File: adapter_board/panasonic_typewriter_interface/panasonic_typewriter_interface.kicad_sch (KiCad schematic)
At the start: 21 parts, among them J1 KMDGX-8S-AS, J2 Conn_02x03_Odd_Even, J3 Connector:Conn_01x05_Male, J4 Connector:Conn_01x04_Male, J5 Connector:Conn_01x04_Male, SW1 SW_SPDT

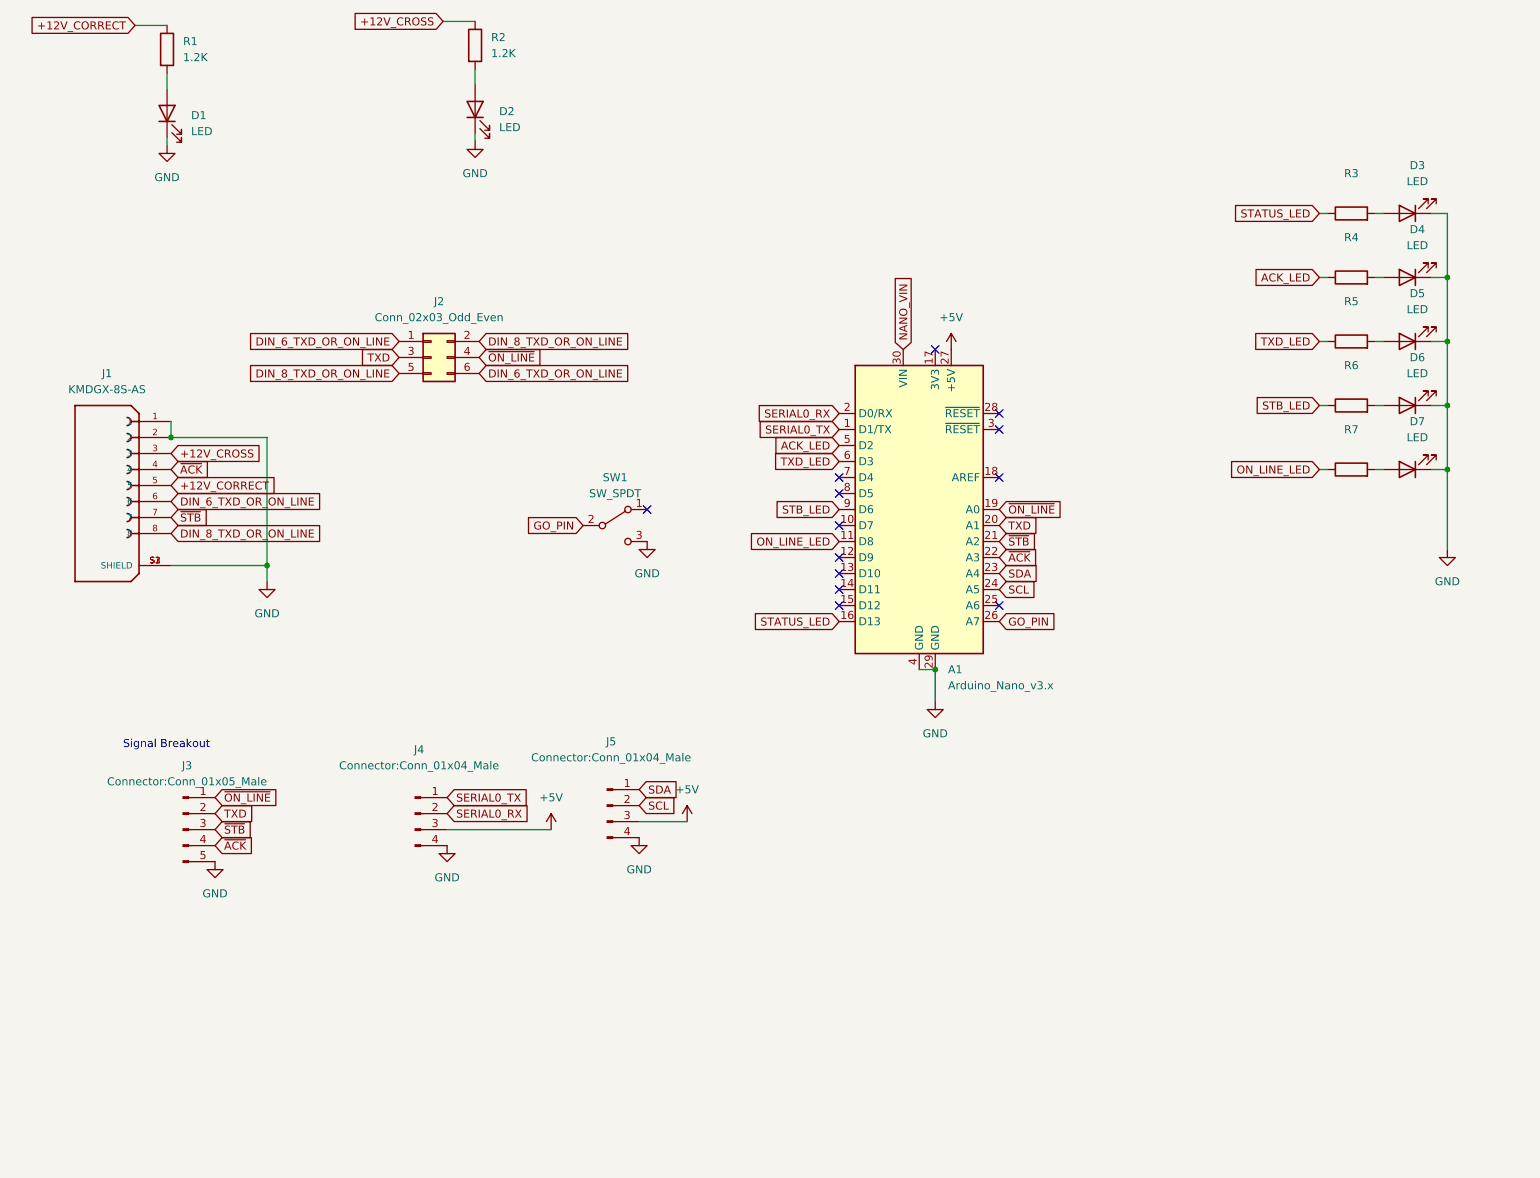
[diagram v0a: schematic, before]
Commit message: slightly larger board with mounting holes and an extra button
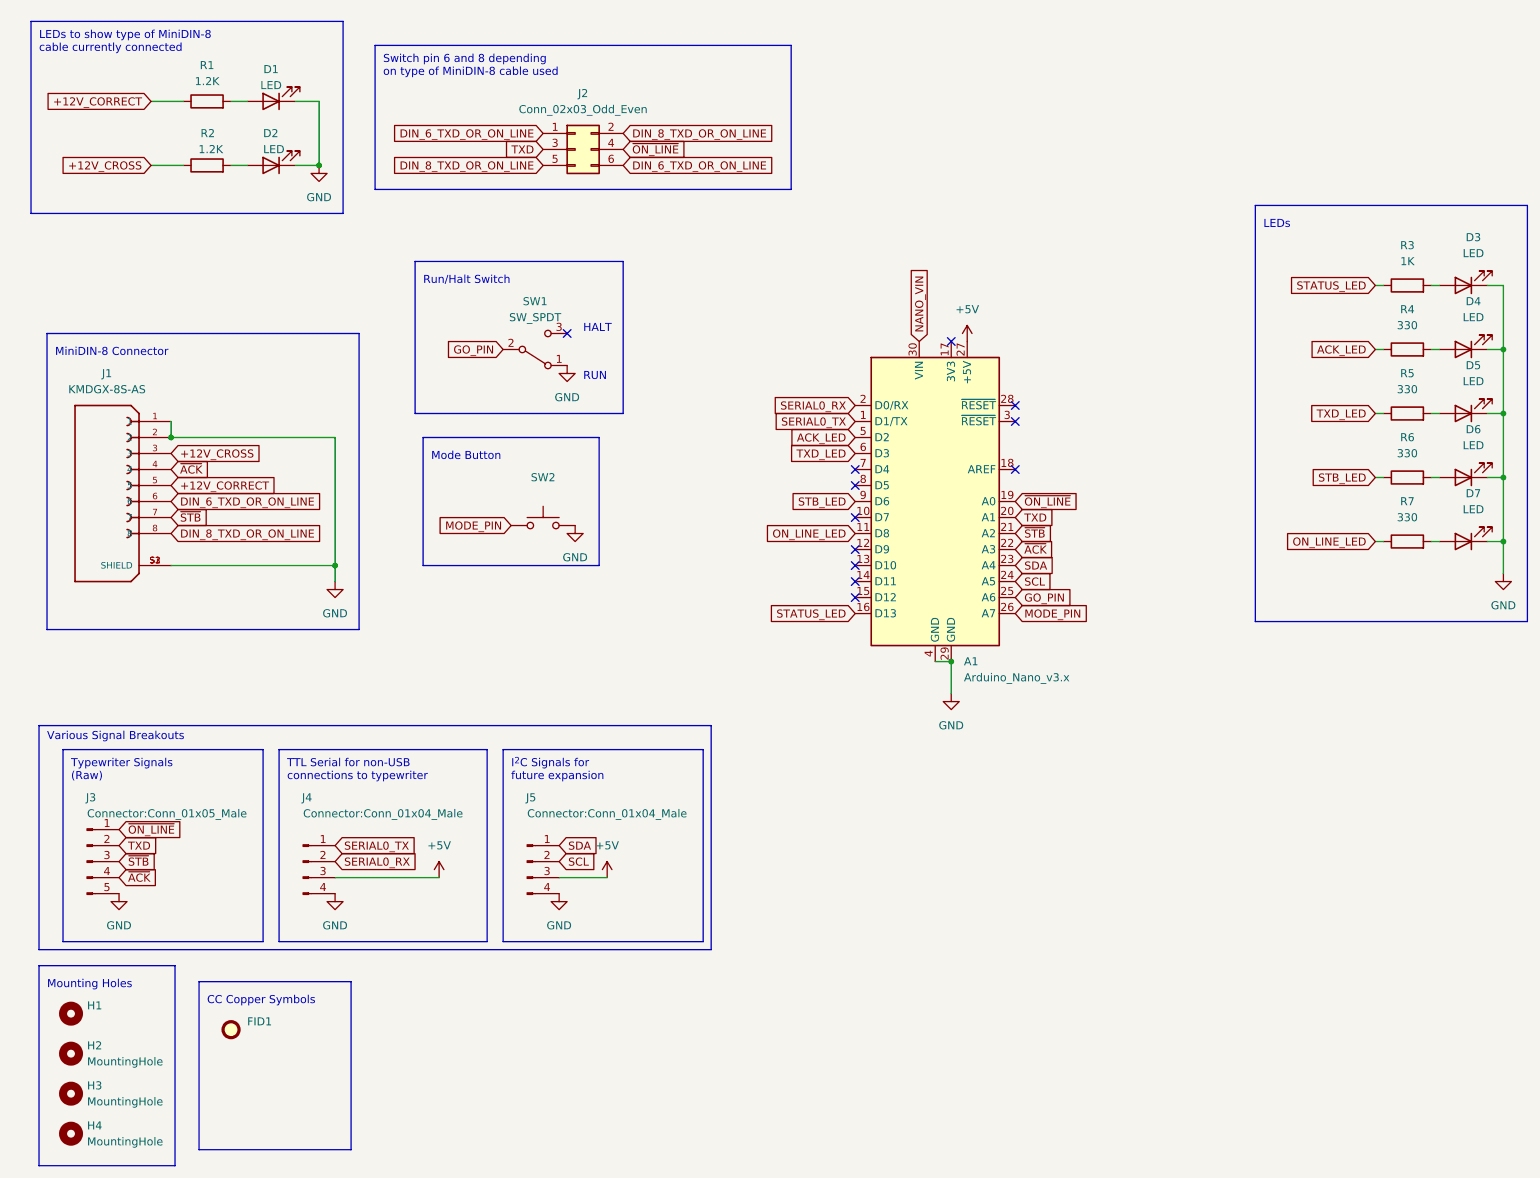
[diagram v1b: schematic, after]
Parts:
- added FID1: (no value), symbol Mechanical:Fiducial
- added H1: (no value), symbol Mechanical:MountingHole
- added H2, H3, H4: MountingHole, MountingHole:MountingHole_2.2mm_M2_DIN965, symbol Mechanical:MountingHole
- added SW2: (no value), symbol Switch:SW_Push
- R3: value (none) -> 1K; footprint (none) -> Resistor_SMD:R_0805_2012Metric
- R4, R5, R6, R7: value (none) -> 330; footprint (none) -> Resistor_SMD:R_0805_2012Metric
- SW1: footprint (none) -> Button_Switch_SMD:SW_SPDT_PCM12
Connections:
- net GND: now also SW1.1 (A), SW2.1; no longer SW1.3 (C)
- net GO_PIN: now also A1.25 (A6); no longer A1.26 (A7)
- new net MODE_PIN: A1.26 (A7), SW2.2
- no-connect marks 13 -> 12
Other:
- note added: "CC Copper Symbols"
- note added: "HALT"
- note added: "I^{2}C Signals for future expansion"
- note added: "LEDs"
- note added: "LEDs to show type of MiniDIN-8 cable currently connected"
- note added: "MiniDIN-8 Connector"
- note added: "Mode Button"
- note added: "Mounting Holes"
- note added: "RUN"
- note added: "Run/Halt Switch"
- note added: "Switch pin 6 and 8 depending on type of MiniDIN-8 cable used"
- note added: "TTL Serial for non-USB connections to typewriter"
- note added: "Typewriter Signals (Raw)"
- note added: "Various Signal Breakouts"
- note removed: "Signal Breakout"
- company: (none) -> github.com/xunker
- title: (none) -> Panasonic Typewriter Interface
- moved on the sheet: A1, D1, D2, D3, D4, D5, D6, D7, J2, J3, J4, J5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

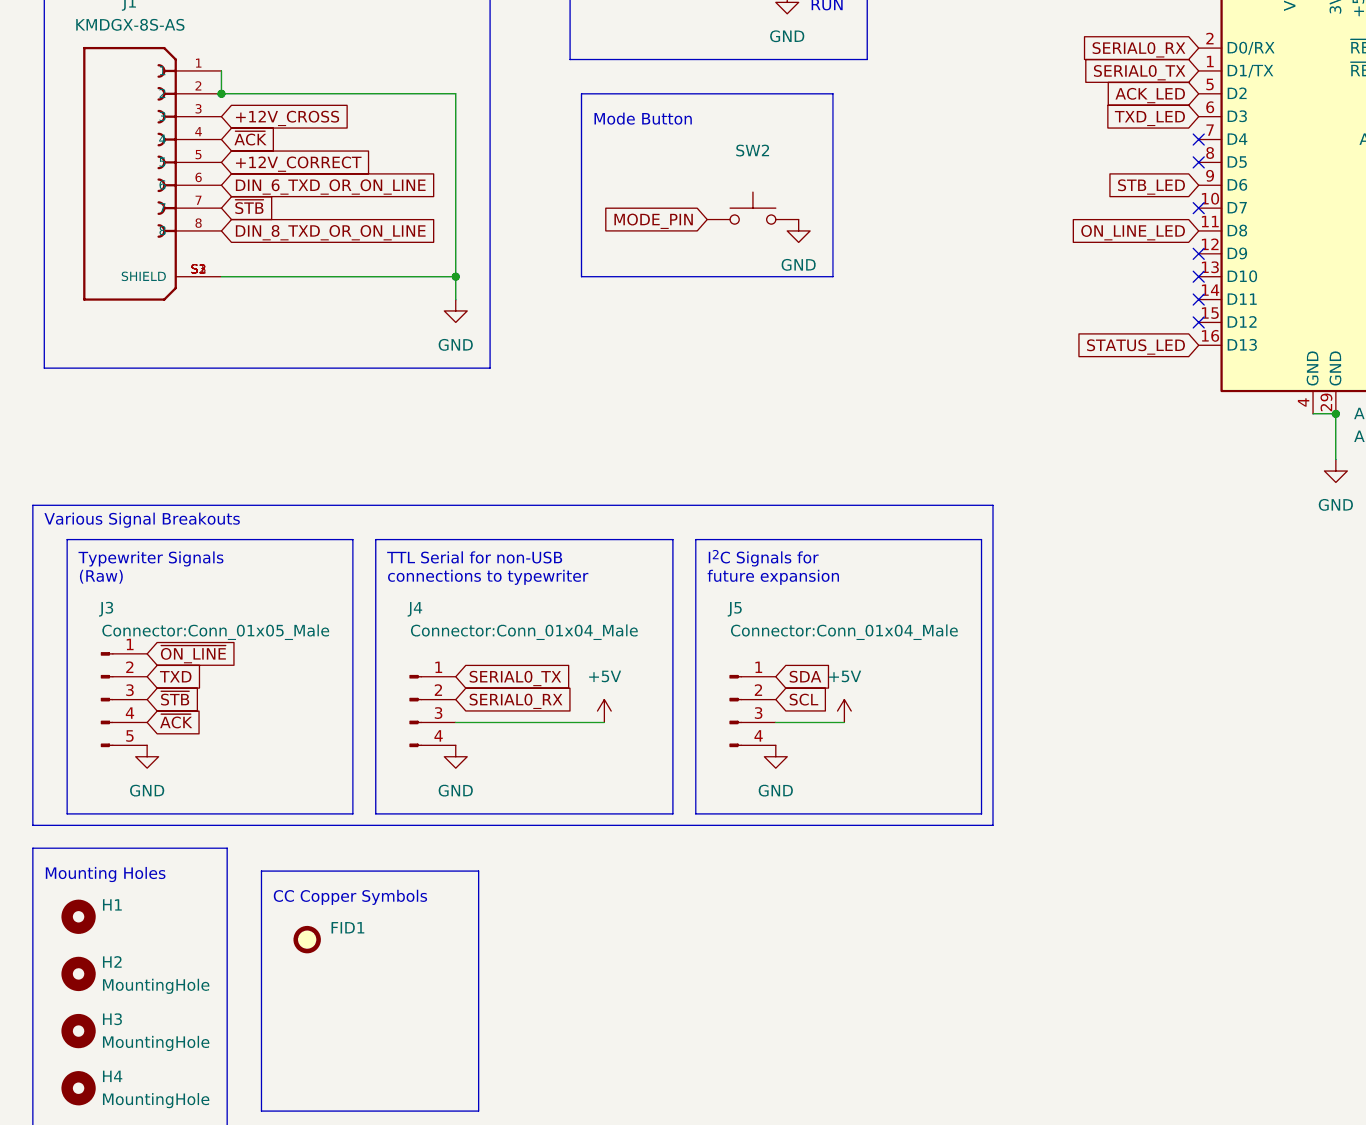
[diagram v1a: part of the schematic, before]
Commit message: Add support for Serial1 on 328PB; change typewriter and serial breakouts to a JST 1.25 connector; changed i2c breakout to be a stemma-compatible jst-sh connector
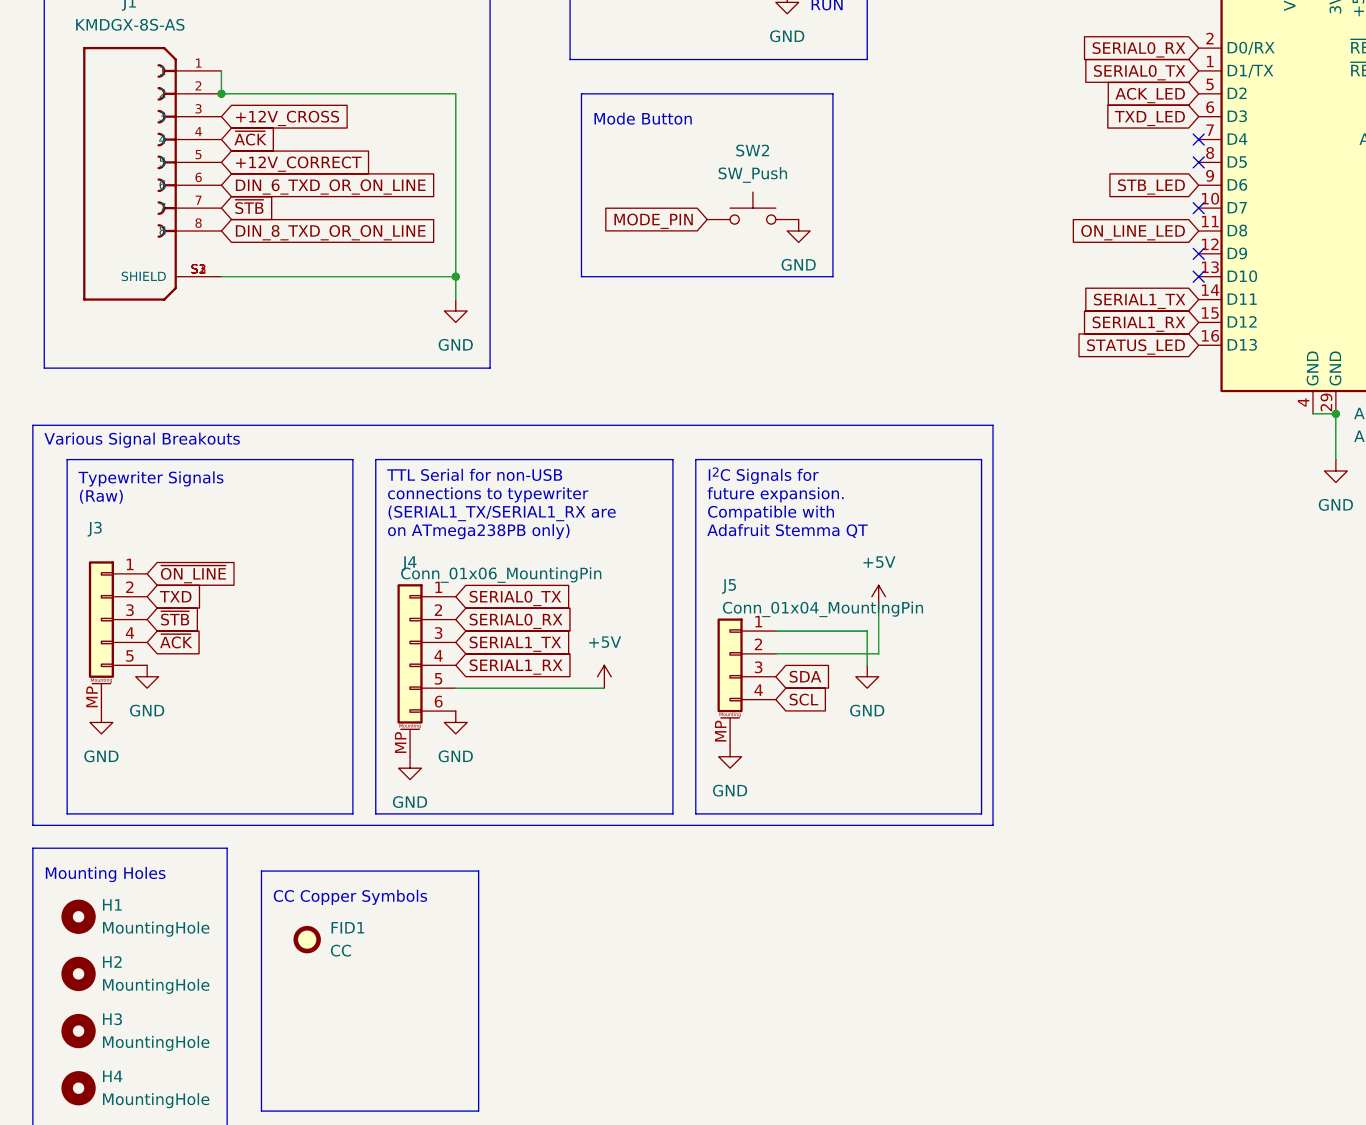
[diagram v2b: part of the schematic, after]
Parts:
- removed J4: Connector:Conn_01x04_Male, Connector_PinHeader_2.54mm:PinHeader_1x04_P2.54mm_Vertical_SMD_Pin1Left, symbol Connector:Conn_01x04_Male
- added J4: Conn_01x06_MountingPin, Connector_JST:JST_GH_SM06B-GHS-TB_1x06-1MP_P1.25mm_Horizontal, symbol Connector_Generic_MountingPin:Conn_01x06_MountingPin
- FID1: value (none) -> CC; footprint (none) -> Symbol:Symbol_CreativeCommons_CopperTop_Type2_Small
- H1: value (none) -> MountingHole; footprint (none) -> MountingHole:MountingHole_2.2mm_M2_DIN965
- J3: value Connector:Conn_01x05_Male -> (none); footprint Connector_PinHeader_2.54mm:PinHeader_1x05_P2.54mm_Vertical_SMD_Pin1Left -> (none); symbol Connector:Conn_01x05_Male -> Connector_Generic_MountingPin:Conn_01x05_MountingPin
- J5: value Connector:Conn_01x04_Male -> Conn_01x04_MountingPin; footprint Connector_PinHeader_2.54mm:PinHeader_1x04_P2.54mm_Vertical_SMD_Pin1Left -> (none); symbol Connector:Conn_01x04_Male -> Connector_Generic_MountingPin:Conn_01x04_MountingPin
- SW2: value (none) -> SW_Push; footprint (none) -> Button_Switch_SMD:SW_SPST_FSMSM
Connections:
- net +5V: now also J5.2 (Pin_2), J4.5 (Pin_5); no longer J5.3 (Pin_3)
- net GND: now also J3.MP (MountPin), J5.1 (Pin_1), J5.MP (MountPin), J4.6 (Pin_6), J4.MP (MountPin); no longer J5.4 (Pin_4)
- net SCL: now also J5.4 (Pin_4); no longer J5.2 (Pin_2)
- net SDA: now also J5.3 (Pin_3); no longer J5.1 (Pin_1)
- net SERIAL0_RX: now also J4.2 (Pin_2)
- net SERIAL0_TX: now also J4.1 (Pin_1)
- net SERIAL1_TX: now reaches A1.14 (D11)
- net SERIAL1_TX: now also J4.3 (Pin_3)
- net SERIAL1_RX: now reaches A1.15 (D12)
- net SERIAL1_RX: now also J4.4 (Pin_4)
- no-connect marks 12 -> 10
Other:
- note added: "I^{2}C Signals for future expansion. Compatible with Adafruit Stemma QT"
- note added: "TTL Serial for non-USB connections to typewriter (SERIAL1_TX/SERIAL1_RX are on ATmega238PB only)"
- note removed: "I^{2}C Signals for future expansion"
- note removed: "TTL Serial for non-USB connections to typewriter"
